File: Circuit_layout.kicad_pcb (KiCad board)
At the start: 2 copper layers, 203.2 x 165.1 mm, 242 parts, among them IC4 TS431ILT, J1 TSV, J10 Conn_01x02, J18 ICSP, J2 CoolingSystem, J21 Lights On Car, J24 Cockpit, J25 RJ11, J3 Pedal, J32 Conn_MC, J34 Can_Iso, J35 GLV_In, J36 GLV_Out, J4 Conn_01x08, J5 Testing Connector, J6 AIRs/SafetyLoop, J7 IMD, J8 DC_Relay, J9 PC_Relay, K1 APAN3105, K2 G6B-1174P-US-DC24, K4 APAN3105, Q1 ZVP0545G, Q2 MMBF170, Q3 ZVP1320F, Q4 STN3NF06L, Q5 SI1302DL-T1-E3, Q8 SI1302DL-T1-E3, SW2 TS5A3159-Q1, SW4 SW_PUSH, U1 RDE03110S12, U10 MCP2551-I/SN, U11 TLP293, U12 TLP293, U13 REF3033, U14 Mounting_hole, U15 Mounting_hole, U16 MCP9700AT-H/TT, U17 Chassis Ground, U18 TS912, U19 74HC00, U2 MCP6002, U20 MC7805BDTRKG, U21 MCP6004, U22 TS372, U23 TLP293, U24 TLP293, U25 NCD9830DBR2G, U27 TLP293, U28 Mounting_hole, U3 MCP6004, U30 DAC5574IDGS, U31 TLP293, U32 TLP293, U37 TLP293, U4 ACPL-C870, U40 MCP6004, U41 PDQ10-Q24-D5-D, U42 LT1763CS8-3.3PBF, U5 SI8600AB-B-IS, U6 TS912, U7 MCP23016, U8 74ACT11030, U9 PIC32MZ2048EFM064-I/PT

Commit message: Version 3 ready for FREEDFM check
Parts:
- added D11: 1N4001, Diodes_THT:D_DO-41_SOD81_P7.62mm_Horizontal, F.Cu at (232.4, 114.6)
- added G***: LOGO, QR:QR_500, F.Cu at (63.0, 108.7)
- added G***: LOGO, QR:QR_500, B.Cu at (62.7, 105.4)
- added G***: LOGO, QR:QR_500, B.Cu at (62.7, 105.7)
- added G***: LOGO, QR:QR, B.Cu at (66.5, 101.6)
- added G***: LOGO, QR:QR, B.Cu at (102.9, 110.5)
- added G***: LOGO, QR:QR, B.Cu at (213.9, 127.5)
- added G***: LOGO, QR:QR, B.Cu at (239.3, 48.8)
- added G***: LOGO, QR:QR, B.Cu at (215.1, 55.1)
- added G***: LOGO, QR:QR, B.Cu at (220.7, 66.0)
- added J11: SL2, Connectors_Molex:Molex_MiniFit-JR-5556-02A_2x01x4.20mm_Straight, F.Cu at (252.0, 114.6)
- added J12: Break_OverTravel, Connectors_Molex:Molex_MiniFit-JR-5556-02A_2x01x4.20mm_Straight, F.Cu at (252.2, 88.4)
- added K3: G6B-1174P-US-DC24, custom_footprints:Relay_SPST_Finder_32.21-x300_special, F.Cu at (237.5, 103.4)
- added R102: 1.6k, Resistors_SMD:R_0805_HandSoldering, F.Cu at (209.6, 50.8)
- added R99: 1.6k, Resistors_SMD:R_0805_HandSoldering, F.Cu at (194.3, 51.3)
- moved J1 5.73 mm to (248.4, 188.0)
- moved C14 2.88 mm to (250.2, 150.1)
- moved Q8 2.75 mm to (209.8, 54.6)
- turned R101 to 180 degrees
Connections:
- net /GLV Interface/SL1 renamed /GLV Interface/SL1_In
- net /GLV Interface/SL1_RTN renamed /GLV Interface/SL1_Out
- J2 pad 5: /CoolTemp_1 -> /CoolTemp_In_1
- J2 pad 7: /CoolTemp_2 -> /CoolTemp_In_2
- J32 pad 3: /Pre-Charge/I/O_ground -> /I/O_Ground
- J36 pad 3: /CH_gnd -> /+24V
- J36 pad 5: /+24V -> /CH_gnd
- JP3 pad 2: /Pre-Charge/I/O_ground -> /I/O_Ground
- R33 pad 2: Net-(R33-Pad2) -> /PC_ready
- U9 pad 17: Net-(U9-Pad17) -> /CoolTemp_1
- U9 pad 18: Net-(U9-Pad18) -> /CoolTemp_2
- U9 pad 44: Net-(U9-Pad44) -> /Break_OverTravel
- U9 pad 48: Net-(U9-Pad48) -> /PC_ready
- U9 pad 49: Net-(U9-Pad49) -> /FlowRate
- U9 pad 50: Net-(U9-Pad50) -> /CoolTemp_1
- U9 pad 51: Net-(U9-Pad51) -> /CoolTemp_2
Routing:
- net /BP_RTN: track 1470.7 -> 1664.5 mm, vias 56 -> 55
- net /Break_OverTravel: track 0.00 -> 101.4 mm, vias 0 -> 4
- net /CH_gnd: track 195.4 -> 262.1 mm, vias 0 -> 2
- net /+24V: track 523.0 -> 549.6 mm, vias 15 -> 13
- net /I/O_Ground: track 492.3 -> 470.7 mm, vias 23 -> 21
- net /CoolTemp_In_2: track 0.00 -> 15.9 mm, vias 0 -> 2
- net /GLV Interface/SL2_Out: track 0.00 -> 14.9 mm
- net /GLV Interface/SL2_In: track 0.00 -> 14.9 mm
- net /CoolTemp_1: track 99.8 -> 112.8 mm, vias 6 -> 7
- net /CoolTemp_In_1: track 0.00 -> 11.1 mm, vias 0 -> 1
- net /Status Lights/TSAL_1: track 216.8 -> 225.1 mm, vias 6 -> 8
- net /BP: track 202.1 -> 195.1 mm, vias 11 -> 12
- net Net-(R68-Pad1): track 6.40 -> 13.0 mm
- net /GLV Interface/CAN_H: track 259.3 -> 253.2 mm
- net Net-(D10-Pad1): track 26.1 -> 31.1 mm, vias 0 -> 2
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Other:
- outline, holes or cut-outs redrawn
- net class Chip added: clearance 0.2, trace_width 0.25, via_dia 0.6, via_drill 0.32
- net class Default: clearance 0.2 -> 0.254
- rule trace_clearance: 0.2 -> 0.254
- board text added: "Cooling Force On"
- board text added: "Cutout zone"
- board text added: "FAQ"
- board text added: "IO_GND"
- board text added: "J32 Pin6"
- board text added: "J32 Pin7"
- board text added: "Motor Controller Force On"
- board text added: "TSI Board Fall 2019 Version III by Feng Qiu Zhengxie Hu Phillip Harding"
- board text removed: "Cooling Force start"
- board text removed: "Motor Controller Relay Jumper"
- board text removed: "TSI Board Fall 2019 Version I by Feng Qiu Zhengxie Hu Phillip Harding"

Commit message: Additional spade connector for Cooling_RTN
Ready for fabrication
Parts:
- removed the G*** at (63.0, 108.7)
- removed the G*** at (62.7, 105.4)
- removed the G*** at (62.7, 105.7)
- removed the G*** at (66.5, 101.6)
- removed the G*** at (102.9, 110.5)
- removed the G*** at (213.9, 127.5)
- removed the G*** at (239.3, 48.8)
- removed the G*** at (215.1, 55.1)
- added G***: LOGO, QR:QR, B.Cu at (218.6, 78.0)
- added J13: Cooling_RTN, 1217861-1:TE_1217861-1, F.Cu at (254.8, 61.0)
- J10: value Conn_01x02 -> CoolingPower
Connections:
- J10 pad 2: /BP_RTN -> /Cooling_power
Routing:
- net /Cooling_power: track 16.7 -> 21.8 mm
- net /BP_RTN: track 1664.5 -> 1661.3 mm, vias 55 -> 54
- net /Status Lights/Drive_LED: track 132.7 -> 129.6 mm
- net /Status Lights/TSAL_1: track 225.1 -> 222.3 mm
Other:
- board text added: "Maintenance Manual"
- board text removed: "FAQ"

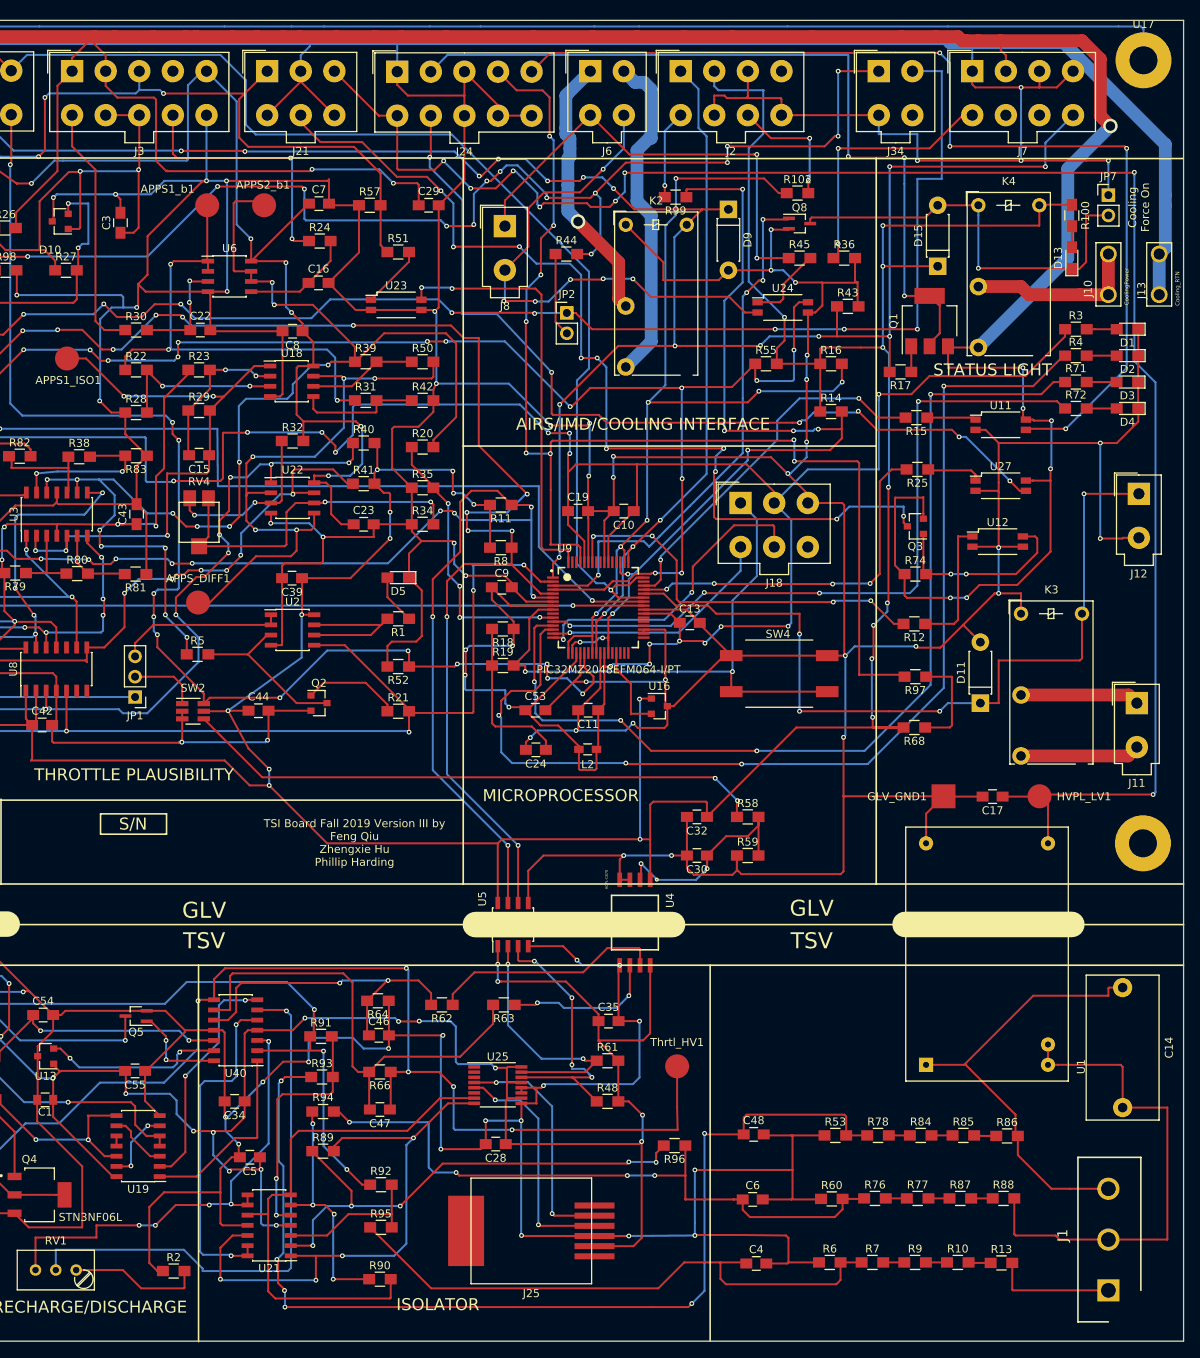
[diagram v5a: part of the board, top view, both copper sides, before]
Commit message: fixing Vref on diff amps
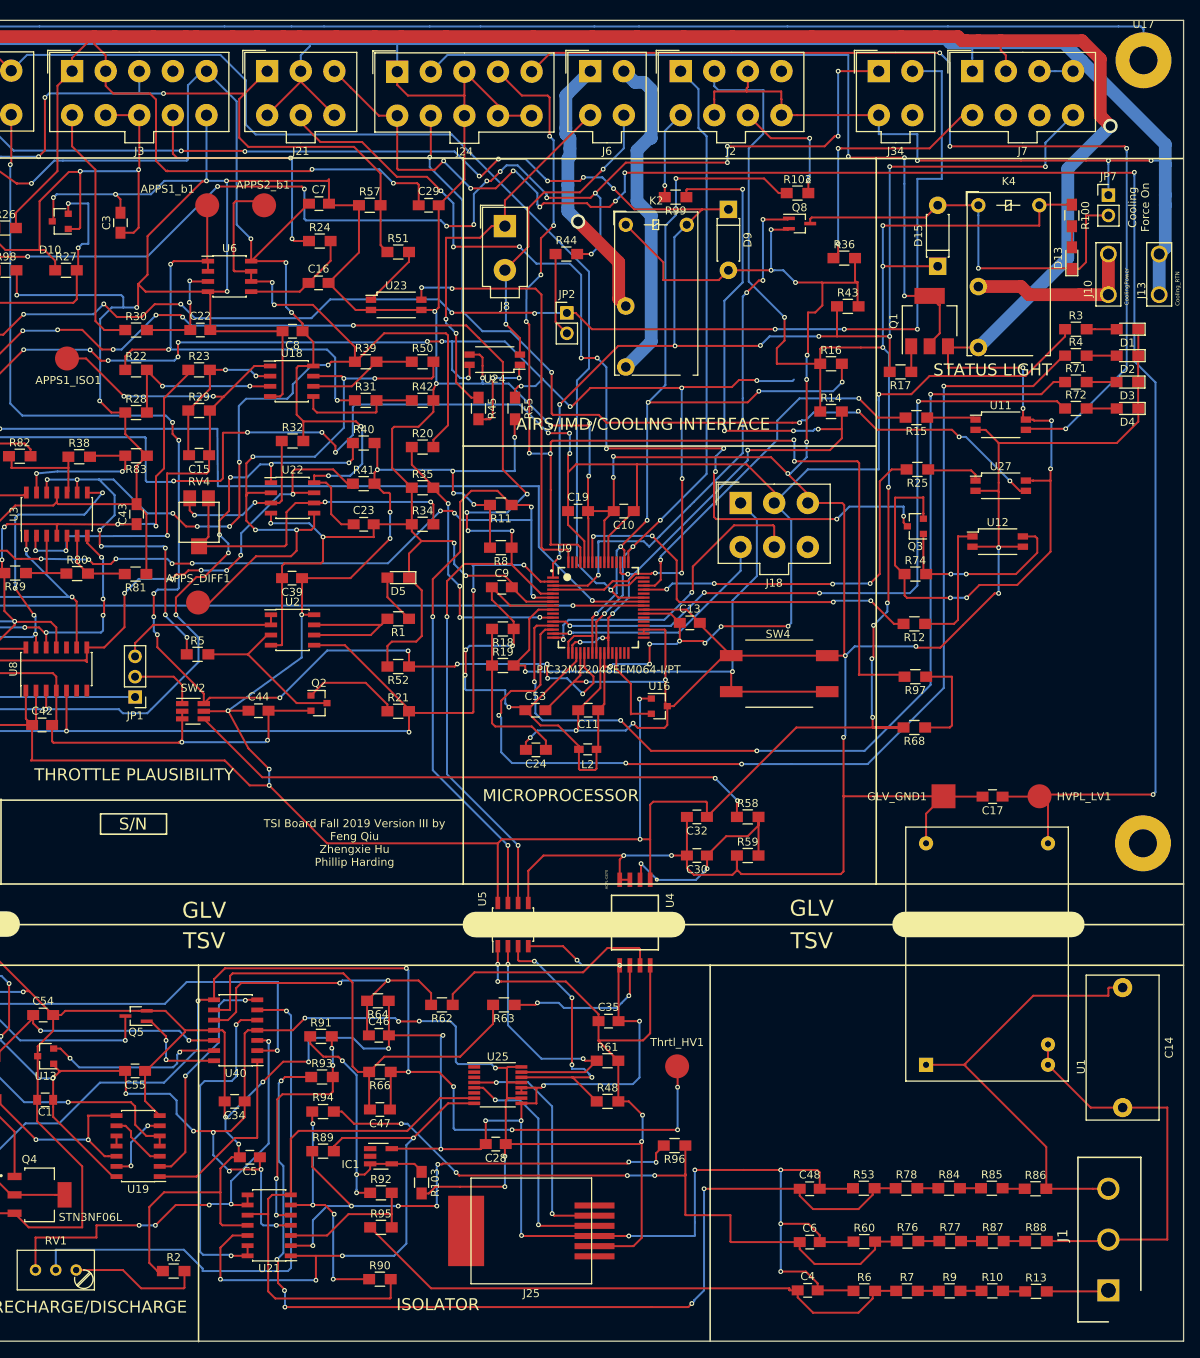
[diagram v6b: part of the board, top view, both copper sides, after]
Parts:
- removed D11: 1N4001, Diodes_THT:D_DO-41_SOD81_P7.62mm_Horizontal
- removed G*** (x2): LOGO, QR:QR
- removed J11: SL2, Connectors_Molex:Molex_MiniFit-JR-5556-02A_2x01x4.20mm_Straight
- removed J12: Break_OverTravel, Connectors_Molex:Molex_MiniFit-JR-5556-02A_2x01x4.20mm_Straight
- removed K3: G6B-1174P-US-DC24, custom_footprints:Relay_SPST_Finder_32.21-x300_special
- added IC1: TS431ILT, TO_SOT_Packages_SMD:SOT-23-5_HandSoldering, F.Cu at (157.5, 171.2)
- added R103: 1k, Resistors_SMD:R_0805_HandSoldering, F.Cu at (162.6, 174.5)
- R55: value 10k -> 2.4k
- moved R45 44.3 mm to (169.7, 77.7), turned to 270 degrees
- moved U24 36.6 mm to (171.7, 71.6), turned to 180 degrees
- moved R55 31.9 mm to (174.2, 77.7), turned to 270 degrees
- moved C48 9.75 mm to (211.1, 175.3)
- moved C6 8.90 mm to (211.1, 181.9)
- moved R53 7.50 mm to (217.8, 175.2)
- moved R86 7.50 mm to (239.3, 175.3)
- moved R78 7.50 mm to (223.2, 175.2)
- moved R84 7.50 mm to (228.5, 175.2)
- moved R85 7.50 mm to (233.8, 175.2)
- moved C4 7.25 mm to (210.8, 188.0)
- moved R88 6.71 mm to (239.4, 181.8)
- moved R60 6.71 mm to (217.9, 181.9)
- moved R76 6.71 mm to (223.3, 181.8)
- moved R77 6.71 mm to (228.6, 181.8)
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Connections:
- R91 pad 1: /+1.24Vref -> /Isolators/DiffAmpRef
- R92 pad 1: /+1.24Vref -> /Isolators/DiffAmpRef
- U9 pad 44: /Break_OverTravel -> Net-(U9-Pad44)
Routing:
- net /Break_OverTravel: track 101.4 -> 0.00 mm, vias 4 -> 0
- net /Isolators/DiffAmpRef: track 0.00 -> 34.3 mm, vias 0 -> 3
- net /BP_RTN: track 1661.3 -> 1628.4 mm, vias 54 -> 52
- net /+1.24Vref: track 145.0 -> 116.6 mm, vias 7 -> 5
- net /AIRs-: track 67.1 -> 40.0 mm, vias 6 -> 2
- net /+5HV: track 331.8 -> 348.0 mm, vias 21 -> 23
- net /GLV Interface/SL2_Out: track 14.9 -> 0.00 mm
- net /GLV Interface/SL2_In: track 14.9 -> 0.00 mm
- net /+5V: track 749.7 -> 764.0 mm, vias 38 -> 39
- net /HV-: track 63.8 -> 52.0 mm
- net /AIRs+: track 58.1 -> 48.5 mm
- net /Isolators/MC+: track 15.6 -> 8.08 mm
- net Net-(C6-Pad1): track 83.5 -> 89.8 mm
- net Net-(C48-Pad1): track 131.8 -> 126.5 mm
- net /I/O_Ground: track 470.7 -> 475.7 mm, vias 21 -> 23
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
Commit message: v3.1
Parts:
- added C20: 0.1u, Capacitors_SMD:C_0805_HandSoldering, F.Cu at (212.6, 166.1)
- added U26: MCP6004, Housings_SOIC:SOIC-14_3.9x8.7mm_Pitch1.27mm, F.Cu at (205.2, 165.9)
- K4: value APAN3105 -> G6B-1174P-US-DC24
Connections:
- C4 pad 2: /I/O_Ground -> /Isolators/DiffAmpRef
- C48 pad 2: /I/O_Ground -> /Isolators/DiffAmpRef
- C6 pad 2: /I/O_Ground -> /Isolators/DiffAmpRef
- R53 pad 1: /I/O_Ground -> /Isolators/DiffAmpRef
- R6 pad 1: /I/O_Ground -> /Isolators/DiffAmpRef
- R60 pad 1: /I/O_Ground -> /Isolators/DiffAmpRef
- R93 pad 1: Net-(C48-Pad1) -> Net-(R93-Pad1)
- R94 pad 1: Net-(C6-Pad1) -> Net-(R94-Pad1)
- R95 pad 1: Net-(C4-Pad1) -> Net-(R95-Pad1)
- R96 pad 1: Net-(C6-Pad1) -> Net-(R94-Pad1)
- U25 pad 10: /+5HV -> Net-(U25-Pad10)
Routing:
- net Net-(R93-Pad1): track 0.00 -> 113.0 mm, vias 0 -> 6
- net /Isolators/DiffAmpRef: track 34.3 -> 144.5 mm, vias 3 -> 9
- net Net-(C48-Pad1): track 126.5 -> 25.0 mm, vias 6 -> 2
- net Net-(R94-Pad1): track 0.00 -> 71.4 mm, vias 0 -> 6
- net Net-(R95-Pad1): track 0.00 -> 69.7 mm, vias 0 -> 2
- net Net-(C6-Pad1): track 89.8 -> 51.0 mm, vias 4 -> 2
- net Net-(C4-Pad1): track 72.3 -> 40.5 mm, vias 0 -> 2
- net /+5HV: track 348.0 -> 376.4 mm, vias 23 -> 25
- net /I/O_Ground: track 475.7 -> 454.0 mm, vias 23 -> 20

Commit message: TSI v4.1
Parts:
- removed JP7: Jumper-Device, Pin_Headers:Pin_Header_Straight_1x02_Pitch2.54mm
- removed K4: G6B-1174P-US-DC24, custom_footprints:Relay_SPST_Finder_32.21-x300_special
- removed Q8: SI1302DL-T1-E3, custom_footprints:SOT-323_SC-70_Handsoldering_special
- removed R100: 500, Resistors_SMD:R_0805_HandSoldering
- added C21: 0.1u, Capacitors_SMD:C_0805_HandSoldering, F.Cu at (210.1, 58.9)
- added C25: 0.1u, Capacitors_SMD:C_0805_HandSoldering, F.Cu at (210.1, 55.4)
- added D11: MMSZ5231B-7-F, Diodes_SMD:D_SOD-123, F.Cu at (232.9, 103.0)
- added D12: MMSZ5231B-7-F, Diodes_SMD:D_SOD-123, F.Cu at (194.6, 154.6)
- added D14: SL Error, LEDs:LED_0805_HandSoldering, F.Cu at (59.2, 118.4)
- added D16: 1N4001, Diodes_THT:D_DO-41_SOD81_P7.62mm_Horizontal, F.Cu at (185.0, 169.1)
- added D17: 1N4001, Diodes_THT:D_DO-41_SOD81_P7.62mm_Horizontal, F.Cu at (75.4, 177.4)
- added G***: LOGO, QR:QR_500, B.Cu at (248.0, 108.8)
- added G***: LOGO, custom_footprints:logo_lafayette_ece_20mmx7mm, F.Cu at (240.9, 109.2)
- added J11: I2C_Testing, 1217861-1:TE_1217861-1, F.Cu at (57.9, 97.8)
- added J12: Conn_01x01, Pin_Headers:Pin_Header_Straight_1x01_Pitch2.54mm, F.Cu at (204.0, 191.3)
- added J14: Conn_01x01, Pin_Headers:Pin_Header_Straight_1x01_Pitch2.54mm, F.Cu at (211.8, 170.9)
- added J15: Conn_01x01, Pin_Headers:Pin_Header_Straight_1x01_Pitch2.54mm, F.Cu at (205.7, 177.9)
- added J16: Conn_01x01, Pin_Headers:Pin_Header_Straight_1x01_Pitch2.54mm, F.Cu at (241.9, 191.3)
- added J17: Conn_01x01, Pin_Headers:Pin_Header_Straight_1x01_Pitch2.54mm, F.Cu at (243.7, 168.9)
- added J19: Conn_01x01, Pin_Headers:Pin_Header_Straight_1x01_Pitch2.54mm, F.Cu at (242.5, 178.8)
- added JP5: Jumper-Device, Pin_Headers:Pin_Header_Straight_1x02_Pitch2.54mm, F.Cu at (56.9, 167.0)
- added JP6: Jumper, Pin_Headers:Pin_Header_Straight_1x02_Pitch2.54mm, F.Cu at (233.9, 56.4)
- added PC_Ready1: Precharge_Ready, Measurement_Points:Measurement_Point_Round-SMD-Pad_Big, F.Cu at (124.0, 185.6)
- added Q6: ZVP1320F, TO_SOT_Packages_SMD:SOT-23, F.Cu at (200.2, 155.1)
- added Q7: ZVP1320F, TO_SOT_Packages_SMD:SOT-23, F.Cu at (239.7, 62.5)
- added R104: 1k, Resistors_SMD:R_0805_HandSoldering, F.Cu at (159.6, 119.3)
- added R105: 500, Resistors_SMD:R_0805_HandSoldering, F.Cu at (153.4, 119.3)
- added R106: 500, Resistors_SMD:R_0805_HandSoldering, F.Cu at (159.6, 122.7)
- added R107: 3k, Resistors_SMD:R_0805_HandSoldering, F.Cu at (153.4, 122.7)
- added R108: 2.4k, Resistors_SMD:R_0805_HandSoldering, F.Cu at (209.8, 133.6)
- added R109: 1M, Resistors_SMD:R_0805_HandSoldering, F.Cu at (194.6, 150.7)
- added R110: 10k, Resistors_SMD:R_0805_HandSoldering, F.Cu at (232.9, 98.4)
- added R111: 10k, Resistors_SMD:R_0805_HandSoldering, F.Cu at (200.8, 150.7)
- added R112: 330, Resistors_SMD:R_0805_HandSoldering, F.Cu at (59.2, 114.4)
- added R113: 10k, Resistors_SMD:R_0805_HandSoldering, F.Cu at (222.3, 58.9)
- added R114: 1M, Resistors_SMD:R_0805_HandSoldering, F.Cu at (233.9, 69.9)
- added SL_TP1: SL_TP, Measurement_Points:Measurement_Point_Round-SMD-Pad_Big, F.Cu at (62.6, 85.6)
- added TSV_Ready1: TSV_Ready, Measurement_Points:Measurement_Point_Round-SMD-Pad_Big, F.Cu at (133.0, 170.1)
- added U29: SN74LVC1G08DCKR, TO_SOT_Packages_SMD:SOT-353_SC-70-5_Handsoldering, F.Cu at (131.6, 180.6)
- added U33: MCP6001, TO_SOT_Packages_SMD:SOT-23-5_HandSoldering, F.Cu at (107.7, 123.1)
- added U34: TLP293, Housings_SSOP:SOP-4_4.4x2.8mm_Pitch1.27mm, F.Cu at (198.4, 142.2)
- added pc_sl1: pc_sl, Measurement_Points:Measurement_Point_Round-SMD-Pad_Big, F.Cu at (136.8, 185.5)
- D13: value LED -> MMSZ5231B-7-F; footprint LEDs:LED_0805_HandSoldering -> Diodes_SMD:D_SOD-123
- R74: value 2.4K -> 1M
- U1: footprint custom_footprints:RDE03110S12 -> custom_footprints:RDE03110S12_new
- moved J8 124.2 mm to (194.2, 177.3)
- moved APPS_DIFF1 37.7 mm to (116.1, 69.2)
- moved Thrtl_HV1 30.9 mm to (163.6, 160.7)
- moved R45 23.7 mm to (171.6, 54.1)
- moved D13 12.2 mm to (233.9, 66.0), turned to 180 degrees
- moved D15 11.5 mm to (234.3, 51.0), turned to 180 degrees
- moved C20 11.3 mm to (204.9, 157.9), turned to 180 degrees
- moved R16 5.84 mm to (213.6, 78.0)
- moved U14 5.08 mm to (252.7, 127.0)
- moved R14 4.95 mm to (213.6, 73.2)
- moved APPS1_ISO1 3.55 mm to (116.1, 74.3)
- moved JP4 3.35 mm to (56.8, 162.6), turned to 180 degrees
- moved J9 2.04 mm to (73.8, 182.6)
- moved APPS2_b1 0.70 mm to (142.8, 53.0)
- moved APPS1_b1 0.70 mm to (135.8, 53.0)
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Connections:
- D13 pad 1: Net-(D13-Pad1) -> /+24V
- D15 pad 1: /+5V -> /Cooling_power
- D15 pad 2: Net-(D13-Pad1) -> /BP_RTN
- J36 pad 3: /+24V -> /CH_gnd
- J36 pad 5: /CH_gnd -> /+24V
- J8 pad 1: /AIRs+ -> /Pre-Charge/DC_Relay+
- J8 pad 2: /AIRs- -> /I/O_Ground
- Q3 pad 1: Net-(Q3-Pad1) -> Net-(D11-Pad2)
- R102 pad 1: /CoolTemp_1 -> /CoolTemp_2
- R11 pad 2: /+5V -> /+3.3V
- R14 pad 1: /+5V -> /+3.3V
- R14 pad 2: /CoolTemp_2 -> /CoolTemp_1
- R16 pad 1: /+5V -> /+3.3V
- R16 pad 2: /CoolTemp_1 -> /CoolTemp_2
- R47 pad 2: /Safety_Loop -> Net-(R47-Pad2)
- R68 pad 2: /+5V -> /+3.3V
- R74 pad 2: Net-(Q3-Pad1) -> Net-(D11-Pad2)
- R8 pad 2: /+5V -> /+3.3V
- R99 pad 1: /CoolTemp_2 -> /CoolTemp_1
- U12 pad 4: Net-(Q3-Pad1) -> Net-(R110-Pad2)
- U19 pad 2: /Pre-Charge/Precharge_Ready -> /Pre-Charge/pc_and_sl_ready
- U20 pad 4: (no net) -> /I/O_Ground
- U5 pad 6: /SDA -> /SCL
- U5 pad 7: /SCL -> /SDA
- U9 pad 1: /IMD_Status -> /IMD_Status_3.3
- U9 pad 2: /Throttle_PL -> /Throttle_PL_3.3
- U9 pad 23: /CoolTemp_1 -> Net-(U9-Pad23)
- U9 pad 24: /FlowRate -> Net-(U9-Pad24)
- U9 pad 27: /CoolTemp_2 -> Net-(U9-Pad27)
- U9 pad 50: /CoolTemp_1 -> Net-(U9-Pad50)
- U9 pad 51: /CoolTemp_2 -> Net-(U9-Pad51)
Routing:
- net /Pre-Charge/+24HV: track 81.1 -> 282.5 mm, vias 1 -> 11
- net /+3.3V: track 398.3 -> 577.7 mm, vias 24 -> 34
- net /AIRs-: track 40.0 -> 191.3 mm, vias 2 -> 8
- net /AIRs+: track 48.5 -> 153.3 mm, vias 2 -> 9
- net /BP_RTN: track 1628.4 -> 1722.5 mm, vias 52 -> 97
- net /IMD_Status: track 243.8 -> 337.2 mm
- net /+5V: track 764.0 -> 692.1 mm, vias 39 -> 47
- net /+5HV: track 376.4 -> 446.3 mm, vias 25 -> 40
- net /I/O_Ground: track 454.0 -> 512.2 mm, vias 20 -> 35
- net Net-(D13-Pad1): track 52.9 -> 0.00 mm, vias 1 -> 0
- net /IMD_Status_3.3: track 0.00 -> 49.3 mm, vias 0 -> 2
- net /Throttle_PL_3.3: track 0.00 -> 45.2 mm, vias 0 -> 2
- net /Pre-Charge/DC_Relay+: track 0.00 -> 39.4 mm, vias 0 -> 4
- net /GLV Interface/CAN_H: track 253.2 -> 217.4 mm, vias 19 -> 10
- net /+24V: track 549.6 -> 585.2 mm, vias 13 -> 22
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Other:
- board text added: "FW"
- board text added: "MC Force On"
- board text added: "PC Force On"
- board text added: "RV"
- board text added: "SL Error"
- board text added: "TSI Board Spring 2020 Version IV by Feng Qiu Zhengxie Hu Phillip Harding"
- board text removed: "IO_GND"
- board text removed: "J32 Pin6"
- board text removed: "J32 Pin7"
- board text removed: "Motor Controller Force On"
- board text removed: "TSI Board Fall 2019 Version III by Feng Qiu Zhengxie Hu Phillip Harding"
